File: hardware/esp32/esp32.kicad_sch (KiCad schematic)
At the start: 66 parts, among them J1 PlugIn_Terminal_01x02, J2 ESP_left, J3 ESP_right, J4 PlugIn_Terminal_01x02, J5 Plugged into C8387, Q4 MMBT5401, Q5 MMBT2222A, U5 LMV321, U6 LM393, U6 LMV321

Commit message: Work on V3.1
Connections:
- net +5V: no longer C6.1
- net 5V_onoff renamed +5Vonoff
- net +5Vonoff: now also C6.1
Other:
- note added: "Additional BoM items:"
- note added: "Alternative 5V input"
- note added: "Alternative? https://www.phoenixcontact.com/de-de/produkte/ leiterplattenstecker-mc-15-2-st-381-1803578"
- note added: "Bus"
- note added: "ESP32 Mini"
- note added: "Main supply is 5V from either USB or 5V input. 3.3V is from ESP, powered by the 5V."
- note added: "Power"
- note added: "Receive"
- note added: "Send"
- note added: "Silkscreen Symbols:"
- note removed: "Supply from USB 5V. To not stress 3.3V from ESP"
- note removed: "V3.1 only"
- note removed: "https://www.phoenixcontact.com/de-de/produkte/leiterplattenstecker-mc-15-2-st-381-1803578"
- moved on the sheet: C10, C12, C14, C15, C16, C17, C19, C21, C24, C27, C31, C33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

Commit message: V3.1: Add power filtering
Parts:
- removed R36: 2k4, Library:R_0603_1608Metric_Pad0.98x0.95mm_HandSolder, symbol symbols:2k4
- added C19, C20: 100u, Library:C_1210_3225Metric_Pad1.33x2.70mm_HandSolder, symbol symbols:100u
- added R37: 18k, Library:R_0603_1608Metric_Pad0.98x0.95mm_HandSolder, symbol symbols:18k
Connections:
- net +3.3V: now also C19.1
- net +5V: now also C20.1
- net GND: now also C19.2, C20.2
- net RX_THRESH: now also R37.2
- net at R22.2, U6.5 (+): now also R37.1
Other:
- note added: "Filter "bad" ESP clone boards power supply to avoid brownout"
- note added: "Vhigh: 1.63V Vlow: 1.33V"
- note added: "~ 0.8V hysteresis"
- moved on the sheet: C14, C31, C33

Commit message: add 100k on hw v3.1
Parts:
- added R32: 100k, Library:R_0603_1608Metric_Pad0.98x0.95mm_HandSolder, symbol symbols:100k
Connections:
- net GND: now also R32.2
- net at C4.2, D1.1 (+), R29.1: now also R32.1
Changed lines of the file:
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@@
   (junction (at 51.435 190.5) (diameter 0) (color 0 0 0 0)
   )
+  (junction (at 41.275 71.12) (diameter 0) (color 0 0 0 0)
+  )
   (junction (at 133.35 53.34) (diameter 0) (color 0 0 0 0)
   )
@@
     (stroke (width 0) (type default))
   )
+  (wire (pts (xy 29.21 74.93) (xy 29.21 71.12))
+    (stroke (width 0) (type default))
+  )
   (wire (pts (xy 111.76 152.4) (xy 118.11 152.4))
     (stroke (width 0) (type default))
@@
     (stroke (width 0) (type default))
   )
-  (wire (pts (xy 41.275 55.88) (xy 41.275 138.43))
+  (wire (pts (xy 41.275 55.88) (xy 41.275 71.12))
     (stroke (width 0) (type default))
   )
@@
     (stroke (width 0) (type default))
   )
+  (wire (pts (xy 41.275 71.12) (xy 41.275 138.43))
+    (stroke (width 0) (type default))
+  )
   (bus (pts (xy 184.15 140.97) (xy 184.15 104.14))
     (stroke (width 0.7) (type default))
@@
     (stroke (width 0) (type default))
   )
+  (wire (pts (xy 29.21 71.12) (xy 41.275 71.12))
+    (stroke (width 0) (type default))
+  )
   (wire (pts (xy 133.35 80.645) (xy 139.7 80.645))
     (stroke (width 0) (type default))
@@
     )
   )
+  (symbol (lib_id "symbols:100k") (at 29.21 78.74 0) (unit 1)
+    (in_bom yes) (on_board yes) (dnp no) (fields_autoplaced)
+    (property "Reference" "R32" (at 31.75 77.47 0)
+      (effects (font (size 1.27 1.27)) (justify left))
+    )
+    (property "Value" "100k" (at 31.75 80.01 0)
+      (effects (font (size 1.27 1.27)) (justify left))
+    )
+    (property "Footprint" "Library:R_0603_1608Metric_Pad0.98x0.95mm_HandSolder" (at 27.432 78.74 90)
+      (effects (font (size 1.27 1.27)) hide)
+    )
+    (property "Datasheet" "~" (at 29.21 78.74 0)
+      (effects (font (size 1.27 1.27)) hide)
+    )
+    (property "MPN" "C25803" (at 29.21 78.74 0)
+      (effects (font (size 1.27 1.27)) hide)
+    )
+    (pin "1")
+    (pin "2")
+    (instances
+      (project "esp32"
+        (path "/a949f3be-99c7-4e8a-a2ba-844ff7c53a70"
+          (reference "R32") (unit 1)
+        )
+      )
+    )
+  )
   (symbol (lib_id "symbols:LMV321") (at 109.22 135.89 0) (mirror y) (unit 1)
     (in_bom yes) (on_board yes) (dnp no)
@@
         )
       )
+    )
+  )
+  (symbol (lib_id "symbols:GND") (at 29.21 82.55 0) (mirror y) (unit 1)
+    (in_bom yes) (on_board yes) (dnp no) (fields_autoplaced)
+    (property "Reference" "#PWR0109" (at 29.21 88.9 0)
+      (effects (font (size 1.27 1.27)) hide)
+    )
+    (property "Value" "GND" (at 29.21 86.36 0)
+      (effects (font (size 1.27 1.27)))
+    )
+    (property "Footprint" "" (at 29.21 82.55 0)
+      (effects (font (size 1.27 1.27)) hide)
+    )
+    (property "Datasheet" "" (at 29.21 82.55 0)
+      (effects (font (size 1.27 1.27)) hide)
+    )
+    (pin "1")
+    (instances
+      (project "stm32"
+        (path "/60790c3a-d4fe-419d-bc96-3387cad42935"
+          (reference "#PWR0109") (unit 1)
+        )
+      )
+      (project "esp32"
+        (path "/a949f3be-99c7-4e8a-a2ba-844ff7c53a70"
+          (reference "#PWR027") (unit 1)
+        )
+      )

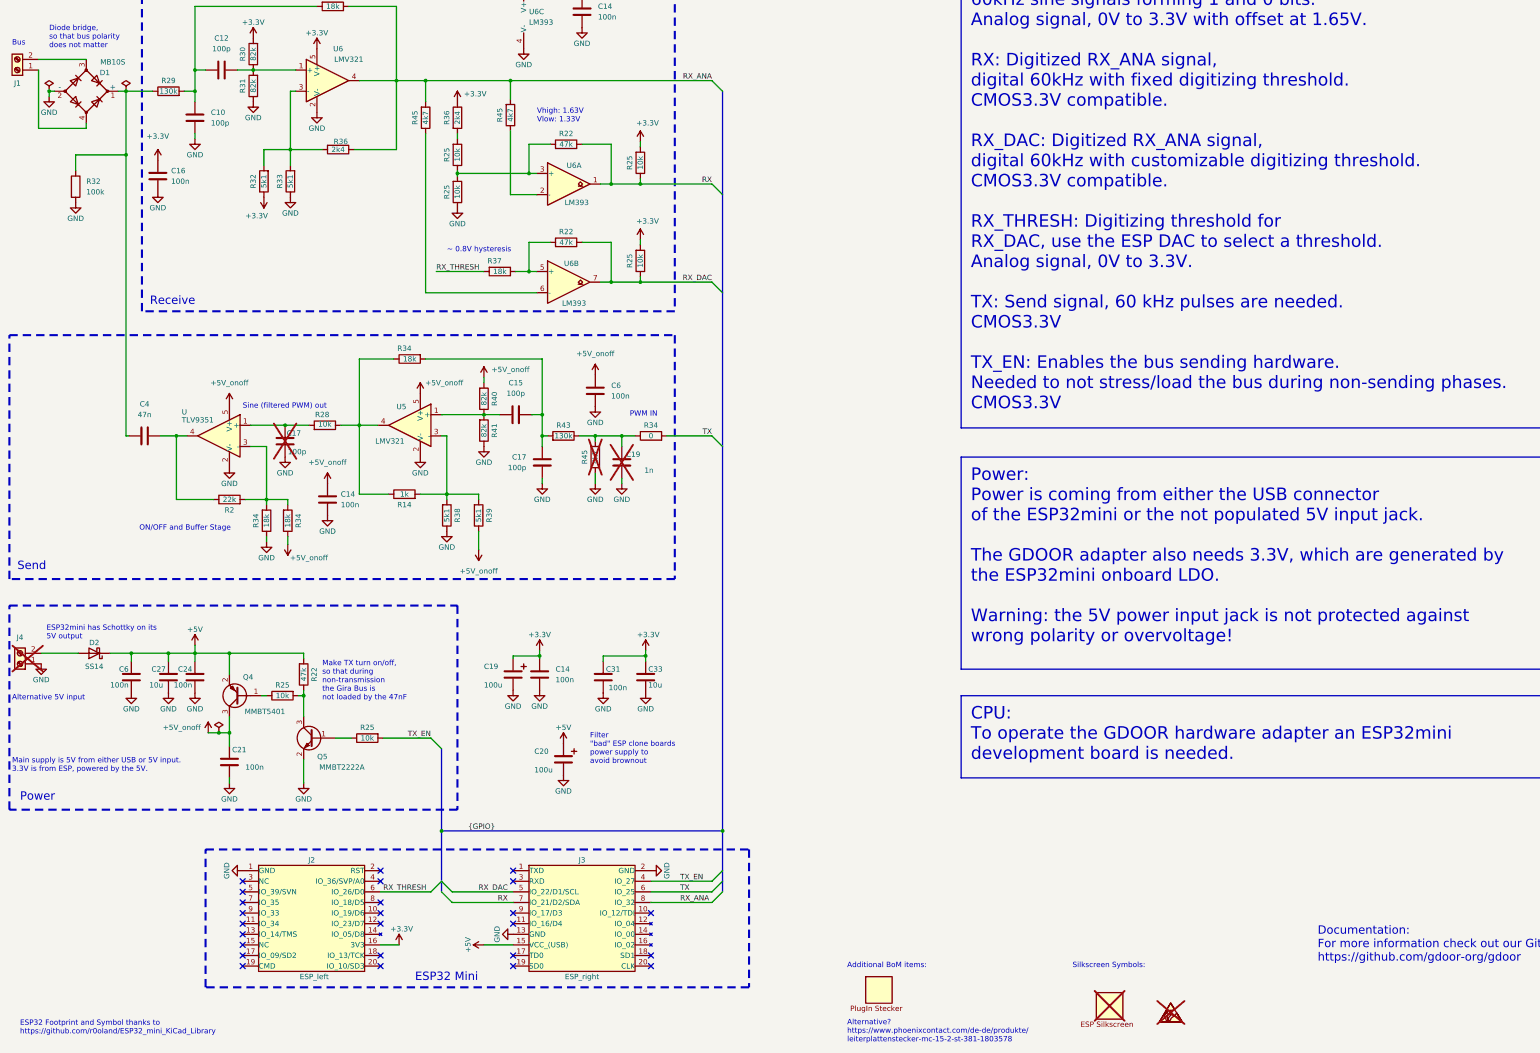
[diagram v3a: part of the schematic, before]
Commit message: Release HW3.1-1
Changed bus connector due to JLCPCB availability
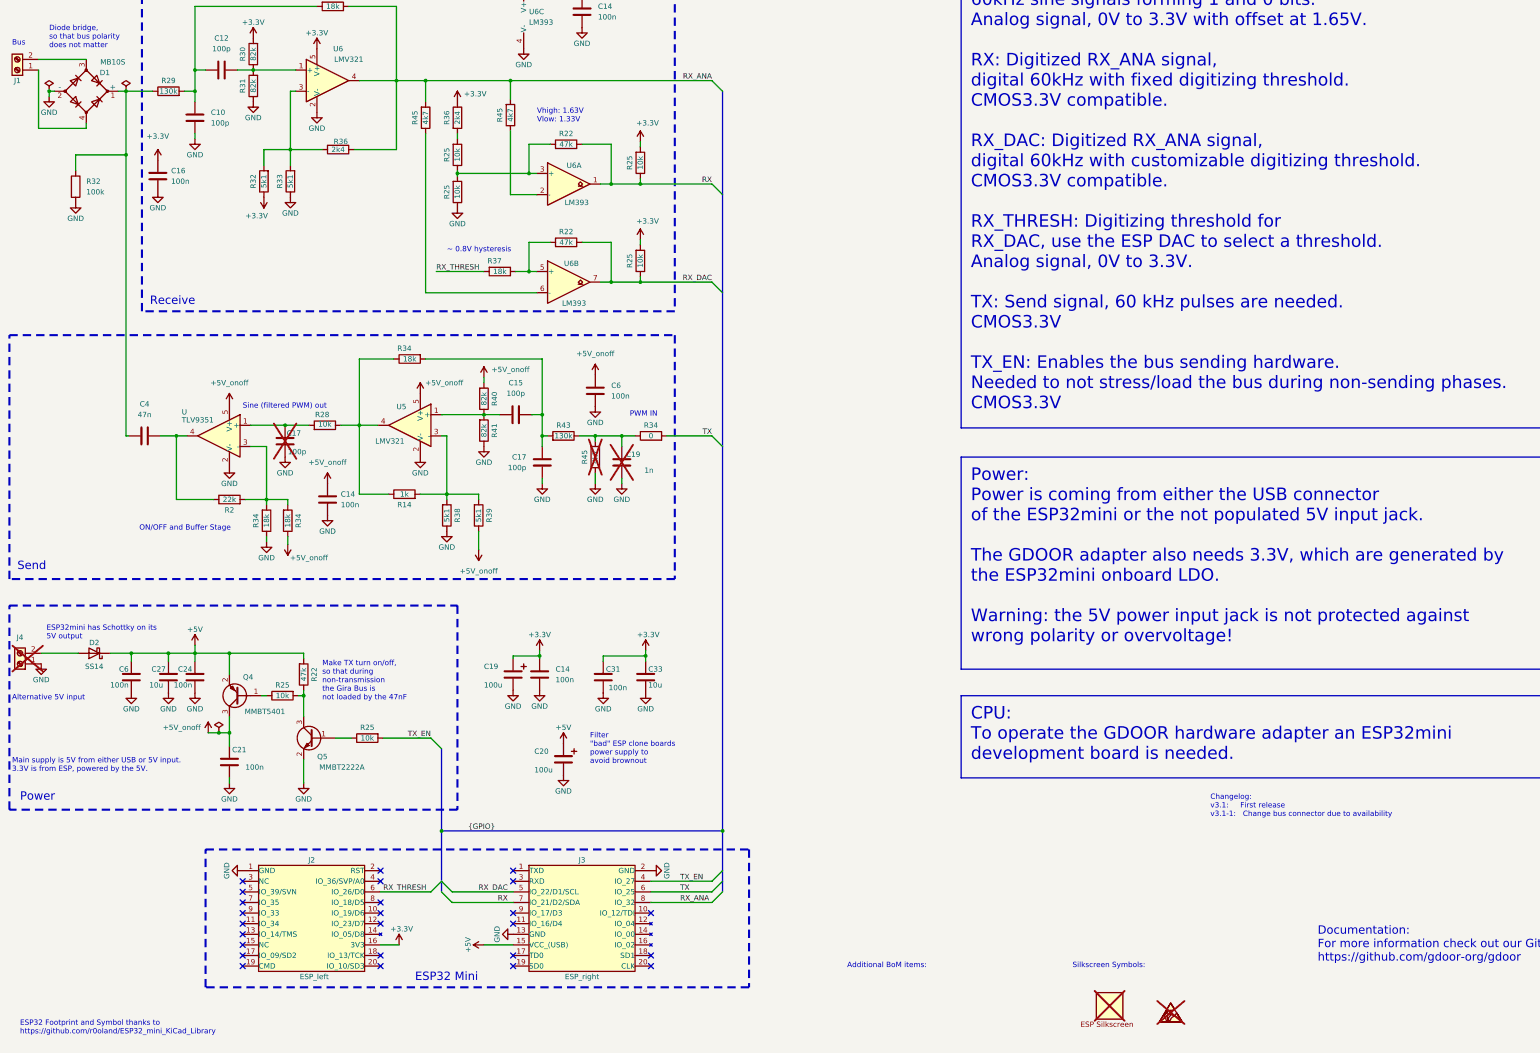
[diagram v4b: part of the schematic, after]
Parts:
- removed J1: PlugIn_Terminal_01x02, Library:steckklemme2x1_1, symbol symbols:PlugIn_Terminal_01x02_1
- removed J5: Plugged into C8387, Library:nofoorprint, symbol symbols:PlugIn Stecker
- added J1: PlugIn_Terminal_Screw, Library:anschlussklemme2x1_3_5, symbol symbols:PlugIn_Terminal_Screw
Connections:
- net at D1.3: now also J1.2 (Pin_2)
- net at D1.4: now also J1.1 (Pin_1)
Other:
- note added: "Changelog: v3.1: First release v3.1-1: Change bus connector due to availability"
- note removed: "Alternative? https://www.phoenixcontact.com/de-de/produkte/ leiterplattenstecker-mc-15-2-st-381-1803578"
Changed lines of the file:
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@@
   (title_block
     (title "ESP32 Mini")
-    (rev "V3.1")
+    (rev "V3.1-1")
   )
   (bus_alias "GPIO" (members "TX_EN" "RX_THRESH" "RX_DAC" "RX" "RX_ANA" "TX"))
@@
     (effects (font (size 1.27 1.27)) (justify left bottom))
   )
-  (text "Alternative?\nhttps://www.phoenixcontact.com/de-de/produkte/\nleiterplattenstecker-mc-15-2-st-381-1803578"
-    (at 213.995 283.845 0)
-    (effects (font (size 1.27 1.27)) (justify left bottom))
-  )
   (text "Diode bridge,\nso that bus polarity\ndoes not matter"
     (at 22.86 45.72 0)
@@
     (effects (font (size 1.27 1.27)) (justify left bottom))
   )
+  (text "Changelog:\nv3.1:     First release\nv3.1-1:   Change bus connector due to availability"
+    (at 300.99 229.87 0)
+    (effects (font (size 1.27 1.27)) (justify left bottom))
+  )
   (text "Bus" (at 13.97 45.085 0)
     (effects (font (size 1.27 1.27)) (justify left bottom))
@@
     )
   )
-  (symbol (lib_id "symbols:PlugIn_Terminal_01x02_1") (at 15.24 50.8 180) (unit 1)
-    (in_bom yes) (on_board yes) (dnp no)
-    (property "Reference" "J1" (at 15.24 53.975 0)
-      (effects (font (size 1.27 1.27)))
-    )
-    (property "Value" "PlugIn_Terminal_01x02" (at 24.13 44.45 0)
-      (effects (font (size 1.27 1.27)) hide)
-    )
-    (property "Footprint" "Library:steckklemme2x1_1" (at 15.24 50.8 0)
-      (effects (font (size 1.27 1.27)) hide)
-    )
-    (property "Datasheet" "https://wmsc.lcsc.com/wmsc/upload/file/pdf/v2/lcsc/1912251632_Ningbo-Kangnex-Elec-WJ15EDGRC-3-81-2P_C8387.pdf" (at 15.24 50.8 0)
-      (effects (font (size 1.27 1.27)) hide)
-    )
-    (property "MPN" "C8387" (at 15.24 50.8 0)
-      (effects (font (size 1.27 1.27)) hide)
-    )
-    (property "JLCPCB Rotation Offset" "90" (at 15.24 50.8 0)
-      (effects (font (size 1.27 1.27)) hide)
-    )
-    (property "JlcRotOffset" "-180" (at 15.24 50.8 0)
-      (effects (font (size 1.27 1.27)) hide)
-    )
-    (pin "1")
-    (pin "2")
-    (instances
-      (project "esp32"
-        (path "/a949f3be-99c7-4e8a-a2ba-844ff7c53a70"
-          (reference "J1") (unit 1)
-        )
-      )
-    )
-  )
-  (symbol (lib_id "symbols:PlugIn Stecker") (at 218.44 267.97 0) (unit 1)
-    (in_bom yes) (on_board yes) (dnp no) (fields_autoplaced)
-    (property "Reference" "J5" (at 218.44 266.7 0)
-      (effects (font (size 1.27 1.27)) hide)
-    )
-    (property "Value" "Plugged into C8387" (at 218.44 267.97 0)
-      (effects (font (size 1.27 1.27)) hide)
-    )
-    (property "Footprint" "Library:nofoorprint" (at 218.44 267.97 0)
-      (effects (font (size 1.27 1.27)) hide)
-    )
-    (property "Datasheet" "https://wmsc.lcsc.com/wmsc/upload/file/pdf/v2/lcsc/1912251636_Ningbo-Kangnex-Elec-WJ15EDGK-3-81-2P_C8466.pdf" (at 218.44 267.97 0)
-      (effects (font (size 1.27 1.27)) hide)
-    )
-    (property "MPN" "C8466" (at 218.44 267.97 0)
-      (effects (font (size 1.27 1.27)) hide)
-    )
-    (instances
-      (project "esp32"
-        (path "/a949f3be-99c7-4e8a-a2ba-844ff7c53a70"
-          (reference "J5") (unit 1)
-        )
-      )
-    )
-  )
   (symbol (lib_id "symbols:GND") (at 89.535 157.48 0) (unit 1)
     (in_bom yes) (on_board yes) (dnp no) (fields_autoplaced)
@@
         )
       )
+    )
+  )
+  (symbol (lib_id "symbols:PlugIn_Terminal_Screw") (at 15.24 50.8 180) (unit 1)
+    (in_bom yes) (on_board yes) (dnp no)
+    (property "Reference" "J1" (at 15.24 53.34 0)
+      (effects (font (size 1.27 1.27)))
+    )
+    (property "Value" "PlugIn_Terminal_Screw" (at 15.24 44.45 0)
+      (effects (font (size 1.27 1.27)) hide)
+    )
+    (property "Footprint" "Library:anschlussklemme2x1_3_5" (at 15.24 50.8 0)
+      (effects (font (size 1.27 1.27)) hide)
+    )
+    (property "Datasheet" "https://wmsc.lcsc.com/wmsc/upload/file/pdf/v2/lcsc/2301061230_DORABO-DB301V-3-5-2P-GN-S_C695629.pdf" (at 15.24 50.8 0)
+      (effects (font (size 1.27 1.27)) hide)
+    )
+    (property "MPN" "C695629" (at 15.24 50.8 0)
+      (effects (font (size 1.27 1.27)) hide)
+    )
+    (property "JLCPCB Rotation Offset" "90" (at 15.24 50.8 0)
+      (effects (font (size 1.27 1.27)) hide)
+    )
+    (property "JlcRotOffset" "-180" (at 15.24 50.8 0)
+      (effects (font (size 1.27 1.27)) hide)
+    )
+    (pin "2")
+    (pin "1")
+    (instances
+      (project "esp32"
+        (path "/a949f3be-99c7-4e8a-a2ba-844ff7c53a70"
+          (reference "J1") (unit 1)
+        )
+      )

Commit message: work on V4.0
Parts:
- removed R32: 100k, Library:R_0603_1608Metric_Pad0.98x0.95mm_HandSolder, symbol symbols:100k
- removed R45: 4k7, Library:R_0603_1608Metric_Pad0.98x0.95mm_HandSolder, symbol symbols:4k7
- added C21: 100u TBD check voltage, Library:C_1210_3225Metric_Pad1.33x2.70mm_HandSolder, symbol symbols:100u
- added C22, C24, C26, C32, C33, C34: 100n, Library:C_0603_1608Metric_Pad1.08x0.95mm_HandSolder, symbol symbols:100n
- added C23, C25, C27, C28, C29, C30, C31, C35, C37, C39, C41, C43, C47, C52, C54, C56: 10u, Library:C_0603_1608Metric_Pad1.08x0.95mm_HandSolder, symbol symbols:10u
- added C36, C38, C40, C42, C46, C51, C53, C55, C62, C63: 100n, Library:C_0402_1005Metric_Pad0.74x0.62mm_HandSolder, symbol symbols:100n_0402
- added C44, C45, C48, C49, C50, C61: 22p, Library:C_0603_1608Metric_Pad1.08x0.95mm_HandSolder, symbol symbols:22p
- added C57, C59: 100u, Library:C_1210_3225Metric_Pad1.33x2.70mm_HandSolder, symbol symbols:100u
- added R27: 18k, Library:R_0603_1608Metric_Pad0.98x0.95mm_HandSolder, symbol symbols:18k
- added R32: 22, Library:R_0603_1608Metric_Pad0.98x0.95mm_HandSolder, symbol symbols:22
- added R35: 82k, Library:R_0603_1608Metric_Pad0.98x0.95mm_HandSolder, symbol symbols:82k
- added R37, R38, R39, R40, R69, R70, R71, R72: 1k, Library:R_0603_1608Metric_Pad0.98x0.95mm_HandSolder, symbol symbols:1k
- added R41, R42, R43, R44, R50, R51, R52, R53, R54: 33, Library:R_0603_1608Metric_Pad0.98x0.95mm_HandSolder, symbol symbols:33
- added R45: 10k, Library:R_0402_1005Metric_Pad0.72x0.64mm_HandSolder, symbol symbols:10k_0402
- added R46, R47: 2k4, Library:R_0603_1608Metric_Pad0.98x0.95mm_HandSolder, symbol symbols:2k4
- added R48, R49: 100, Library:R_0603_1608Metric_Pad0.98x0.95mm_HandSolder, symbol symbols:100
- added R55, R56, R57, R58, R59, R60, R61, R62, R63, R64, R65, R66, R67, R68: 0, Library:R_0603_1608Metric_Pad0.98x0.95mm_HandSolder, symbol symbols:0R
- added R73: 10k, Library:R_0603_1608Metric_Pad0.98x0.95mm_HandSolder, symbol symbols:10k
- added U5: ES8374, Library:QFN-28-1EP_4x4mm_P0.4mm_EP2.3x2.3mm, symbol symbols:ES8374
- added unit 2 of U5
- added unit 3 of U5
- added unit 4 of U5
- added U7: AMS1117-3.3, Library:SOT-223-3_TabPin2, symbol symbols:AMS1117-3.3
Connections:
- net +3.3V: now also R46.1, R47.1, R55.2
- net +5V: now also R57.2
- net GND: now also R37.2, C22.2, C23.1, C24.2, C25.1, C26.2, C27.1, C32.2, C33.2, C34.2, C35.1, C36.1, C37.1, C38.1, C39.1, C40.1, C41.1, C42.1, C43.1, C44.1, C45.1, C46.1, C47.1, C48.1, C49.1, C50.1, C51.1, C52.1, C53.1, C54.1, C55.1, C56.1, C57.2, C59.2, C61.1, R27.2, R45.1, R59.1, R60.1, R61.1, R62.1, R67.1, R68.1, R69.1, R70.1, R71.1, R72.1, R73.2, U5.12 (SPKGND), U5.17 (AGND), U5.29 (EP), U5.3 (DGND), U7.1 (GND)
- net RX_DAC: now also R56.2; no longer R22.1, R25.1, U6.7
- net TX: now also J3.10 (IO_12/TDI); no longer J3.6 (IO_25)
- net at U6.6 (-): now also R27.1
- net I2S_MCLK: now reaches J3.14 (IO_00)
- net I2S_MCLK: now also R50.1
- net at C4.2, D1.1 (+), R29.1: now also C21.2, C28.2, C29.2, C30.2, C31.2, R35.2
- net I2S_SCLK: now reaches J2.14 (IO_05/D8)
- net I2S_SCLK: now also R52.1
- net I2S_ASDOUT: now reaches J2.7 (IO_35)
- net I2S_ASDOUT: now also R53.1
- net RX_THRESH renamed I2S_DSDIN
- net I2S_DSDIN: now also R54.1; no longer R37.2
- new net: C31.1, C62.2, R40.1, R61.2, R65.2
- new net: C42.2, C43.2, R41.1, U5.16 (AVDD)
- new net: C40.2, C41.2, R42.1, U5.6 (DVDD)
- new net: C45.2, R49.2, U5.28 (CDATA)
- new net: C46.2, C47.2, C51.2, C52.2, C53.2, C54.2, C55.2, C56.2, R41.2, R42.2, R43.2, R44.2, R55.1, R58.1
- new net: R22.1, R25.1, R56.1, U6.7
- new net: C44.2, R48.2, U5.1 (CCLK)
- new net: C33.1, C57.1, R57.1, U7.3 (VI)
- new net: C30.1, C62.1, R39.1, R59.2, R64.2
- new net: R39.2, R70.2, U5.22 (MIC2N)
- new net: R38.2, R71.2, U5.25 (MIC1P)
- new net: R53.2, U5.8 (ASDOUT)
- new net: C36.2, C37.2, R44.1, U5.13 (SPKVDD)
- new net: R54.2, U5.10 (DSDIN)
- new net: C25.2, C26.1, U5.19 (ADCVREF)
- new net: C22.1, C35.2, U5.21 (MICBIAS)
- new net: C27.2, C34.1, U5.18 (DACVREF)
- new net: R68.2, U5.11 (SPKN)
- new net: R67.2, U5.14 (SPKP)
- new net: R32.1, U5.15 (MONOOUT)
- new net: C23.2, C24.1, U5.20 (VMID)
- new net: R40.2, R69.2, U5.23 (MIC2P)
- new net: R37.2, R72.2, U5.24 (MIC1N)
- new net: C28.1, C63.1, R37.1, R60.2, R63.2
- new net: C29.1, C63.2, R38.1, R62.2, R66.2
- new net: C38.2, C39.2, R43.1, U5.5 (PVDD)
- new net: C48.2, R52.2, U5.7 (SCLK)
- new net: R45.2, U5.27 (CE)
- new net: C50.2, R50.2, U5.2 (MCLK)
- new net: C21.1, R32.2
- new net: C49.2, R51.2, U5.9 (LRCK)
- new net +3.3V_ANA: C32.1, C59.1, C61.2, R58.2, R63.1, R64.1, R65.1, R66.1, U7.2 (VO)
- new net BUS_DCVOLT: R35.1, R73.1
- new net I2C_SCLK: R47.2, R48.1
- new net I2C_SDA: R46.2, R49.1
- new net I2S_LRCK: J3.6 (IO_25), R51.1
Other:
- note added: "Changelog: v3.1: First release v3.1-1: Change bus connector due to availability v4.0: Audio Support"
- note added: "TODO: Connect Bus DC volt"
- note added: "TODO: check that it works without DAC"
- note removed: "Changelog: v3.1: First release v3.1-1: Change bus connector due to availability"
- note removed: "~ 0.8V hysteresis"
